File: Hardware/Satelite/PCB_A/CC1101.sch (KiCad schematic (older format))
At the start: 19 parts, among them U2 CC1101RGP, U3 0915BM15A0001E, Y1 26 MHz

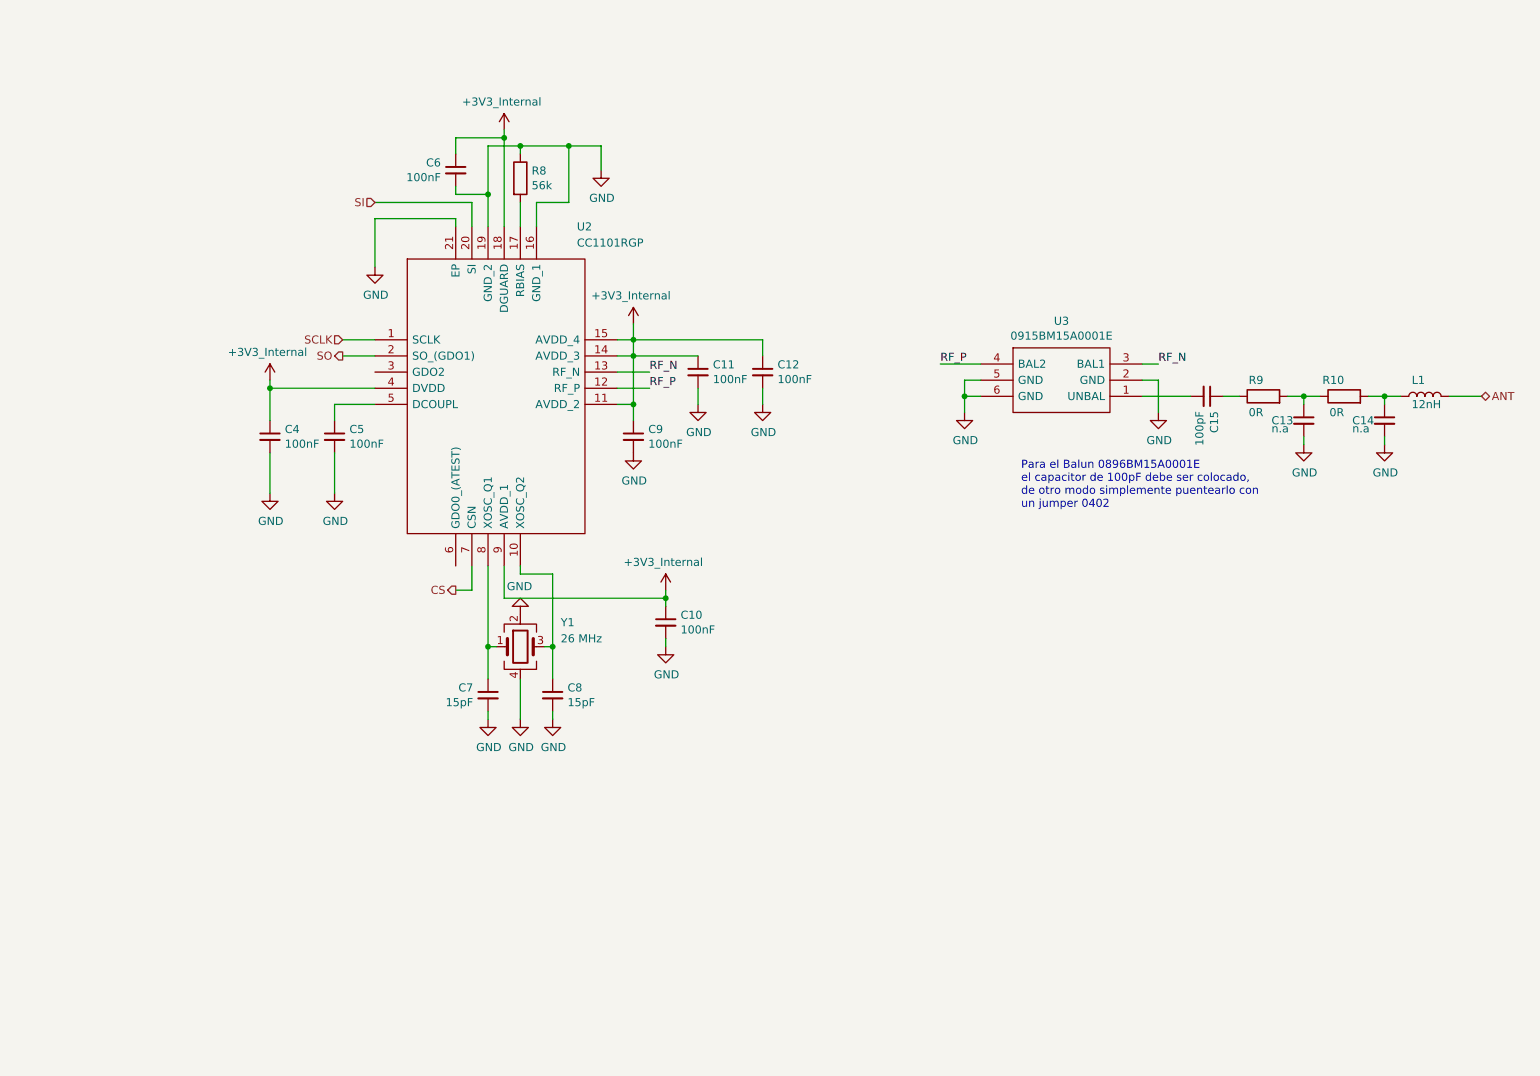
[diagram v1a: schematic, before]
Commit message: Agregado extensor de rango CC1190 en PCB_A
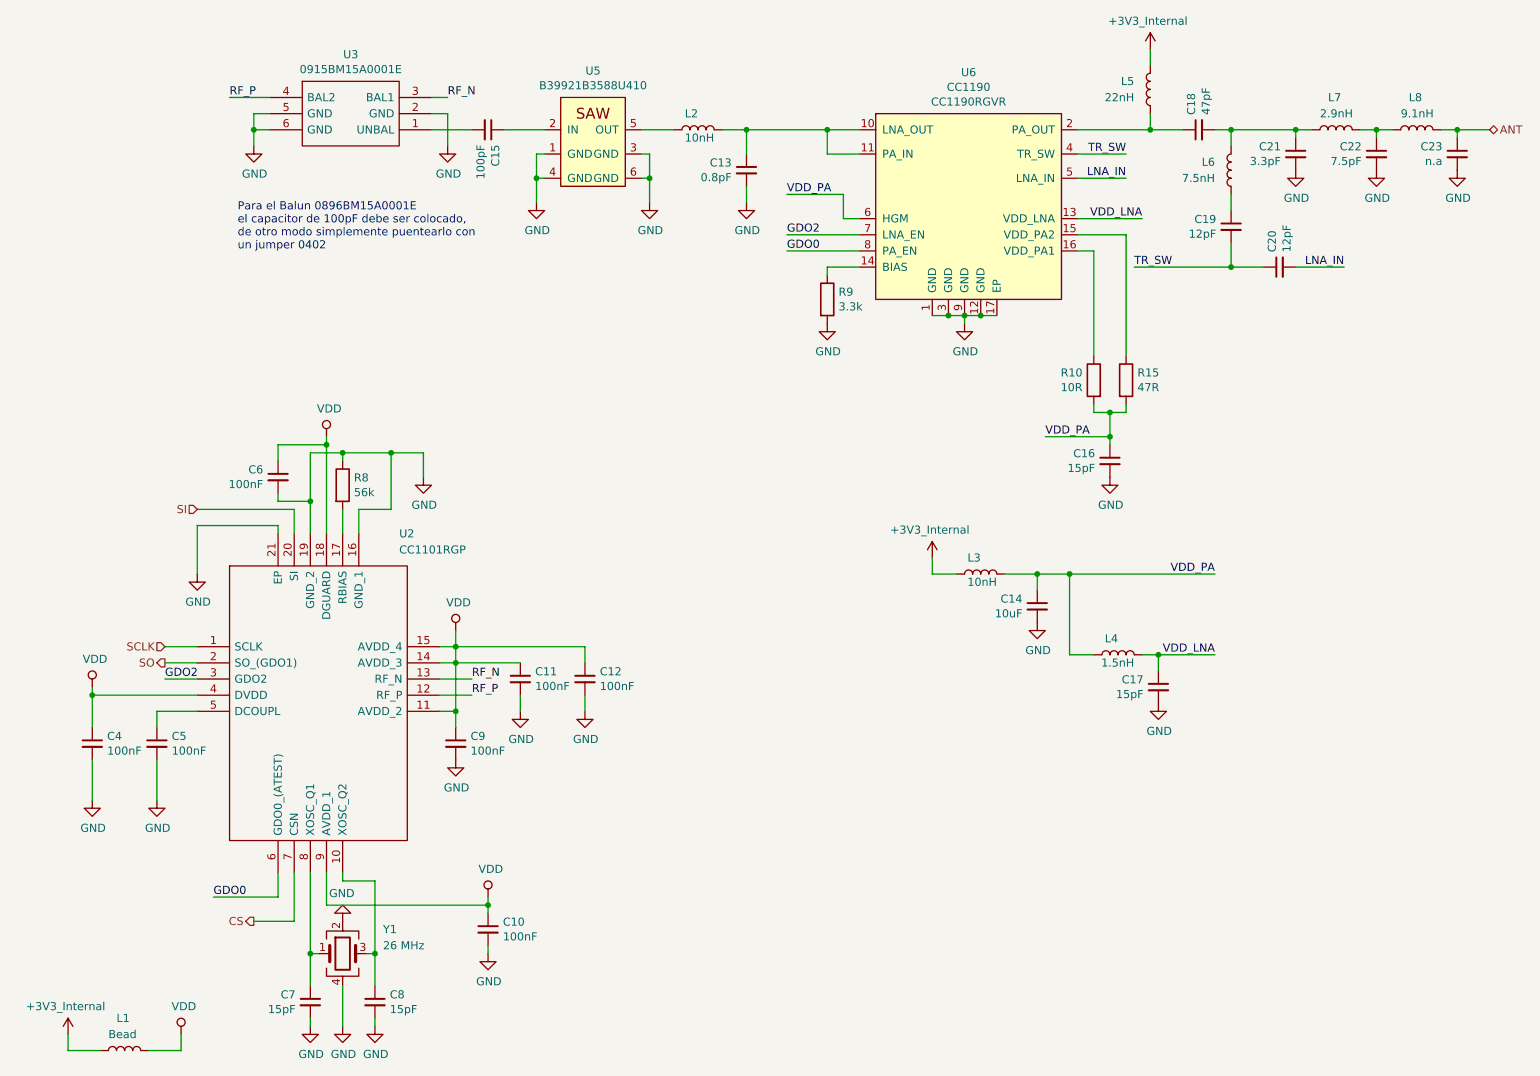
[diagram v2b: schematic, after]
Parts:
- added C16, C17: 15pF, Capacitor_SMD:C_0402_1005Metric, symbol Device:C_Small
- added C18: 47pF, Capacitor_SMD:C_0402_1005Metric, symbol Device:C_Small
- added C19, C20: 12pF, Capacitor_SMD:C_0402_1005Metric, symbol Device:C_Small
- added C21: 3.3pF, Capacitor_SMD:C_0402_1005Metric, symbol Device:C_Small
- added C22: 7.5pF, Capacitor_SMD:C_0402_1005Metric, symbol Device:C_Small
- added C23: n.a, Capacitor_SMD:C_0402_1005Metric, symbol Device:C_Small
- added L2, L3: 10nH, Inductor_SMD:L_0402_1005Metric, symbol Device:L
- added L4: 1.5nH, Inductor_SMD:L_0402_1005Metric, symbol Device:L
- added L5: 22nH, Inductor_SMD:L_0603_1608Metric_Pad1.05x0.95mm_HandSolder, symbol Device:L
- added L6: 7.5nH, Inductor_SMD:L_0402_1005Metric, symbol Device:L
- added L7: 2.9nH, Inductor_SMD:L_0402_1005Metric, symbol Device:L
- added L8: 9.1nH, Inductor_SMD:L_0402_1005Metric, symbol Device:L
- added R15: 47R, Resistor_SMD:R_0402_1005Metric, symbol Device:R
- added U5: B39921B3588U410, AXTEC:B39921B3588U410, symbol AXTEC_IC:B39921B3588U410
- added U6: CC1190, Package_DFN_QFN:Texas_S-PVQFN-N16_EP2.7x2.7mm, symbol AXTEC_IC:CC1190
- C13: value n.a -> 0.8pF; Dielectric (none) -> NP0; Manufacturer Part Number (none) -> GRM1555C2AR80BA01D
- C14: value n.a -> 10uF; footprint Capacitor_SMD:C_0402_1005Metric -> Capacitor_SMD:C_0805_2012Metric_Pad1.15x1.40mm_HandSolder; Dielectric (none) -> NP0; Manufacturer Part Number (none) -> C2012X7R1A106M125AC
- L1: value 12nH -> Bead; Manufacturer Part Number L-07C12NJV6 -> BLM15HG102SN1D
- R10: value 0R -> 10R; Manufacturer Part Number RC0402JR-070RL -> RC0402FR-0710RL
- R9: value 0R -> 3.3k; Manufacturer Part Number RC0402JR-070RL -> RC0402FR-073K3L
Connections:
- net +3V3_Internal: now also L1.2, L3.1, L5.1; no longer C10.1, C11.1, C12.1, C4.1, C6.1, C9.1, U2.11 (AVDD_2), U2.14 (AVDD_3), U2.15 (AVDD_4), U2.18 (DGUARD), U2.4 (DVDD), U2.9 (AVDD_1)
- net ANT: now also C23.1, L8.1; no longer L1.2
- net GND: now also R9.2, C16.2, C17.2, C21.2, C22.2, C23.2, U5.1 (GND), U5.3 (GND), U5.4 (GND), U5.6 (GND), U6.1 (GND), U6.12 (GND), U6.17 (EP), U6.3 (GND), U6.9 (GND)
- net at C15.1: now also U5.2 (IN); no longer R9.1
- net VDD_PA: now reaches C14.1, R10.2
- net VDD_PA: now also C16.1, L3.2, L4.1, R15.2, U6.6 (HGM); no longer L1.1
- net GDO2: now reaches U2.3 (GDO2)
- net GDO2: now also U6.7 (LNA_EN)
- net GDO0: now reaches U2.6 (GDO0_(ATEST))
- net GDO0: now also U6.8 (PA_EN)
- new net: L2.1, U5.5 (OUT)
- new net: C13.1, L2.2, U6.10 (LNA_OUT), U6.11 (PA_IN)
- new net: C18.1, L5.2, U6.2 (PA_OUT)
- new net: C18.2, C21.1, L6.1, L7.2
- new net: C19.1, L6.2
- new net: C22.1, L7.1, L8.2
- new net: R9.1, U6.14 (BIAS)
- new net: R15.1, U6.15 (VDD_PA2)
- new net: R10.1, U6.16 (VDD_PA1)
- new net LNA_IN: C20.2, U6.5 (LNA_IN)
- new net TR_SW: C19.2, C20.1, U6.4 (TR_SW)
- new net VDD: C10.1, C11.1, C12.1, C4.1, C6.1, C9.1, L1.1, U2.11 (AVDD_2), U2.14 (AVDD_3), U2.15 (AVDD_4), U2.18 (DGUARD), U2.4 (DVDD), U2.9 (AVDD_1)
- new net VDD_LNA: C17.1, L4.2, U6.13 (VDD_LNA)
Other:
- moved on the sheet: C10, C11, C12, C15, C4, C5, C6, C7, C8, C9, R8, U2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
